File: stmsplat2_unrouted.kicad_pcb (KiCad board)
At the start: 2 copper layers, 100 x 100 mm, 107 parts, among them J1 C11_2X36, J10 Conn_01x03_Male, J11 Conn_01x02_Male, J12 Conn_01x04_Male, J13 Conn_01x04_Male, J14 Conn_01x02, J15 Conn_01x02, J16 Screw_Terminal_01x03, J17 Screw_Terminal_01x02, J2 C12_2X36, J3 Conn_01x04_Male, J4 Conn_01x04_Male, J5 Conn_Coaxial, J6 Conn_01x04_Male, J7 Conn_01x04_Male, J8 Conn_01x04_Male, J9 Conn_01x03_Male, Q1 BSS138LT1G, U1 ublox_chinese_PCB_module, U10 XCVR_E30-400M20S (Si4463), U11 3115_module, U2 ESP-C3-13U, U3 SST25VF032B, U4 48L512-48LM01, U5 Opamp_Quad_MCP6024, U6 E180-ZG120A, U7 AZ1084C, U8 MCP6S93-X_UN, U9 DS2485

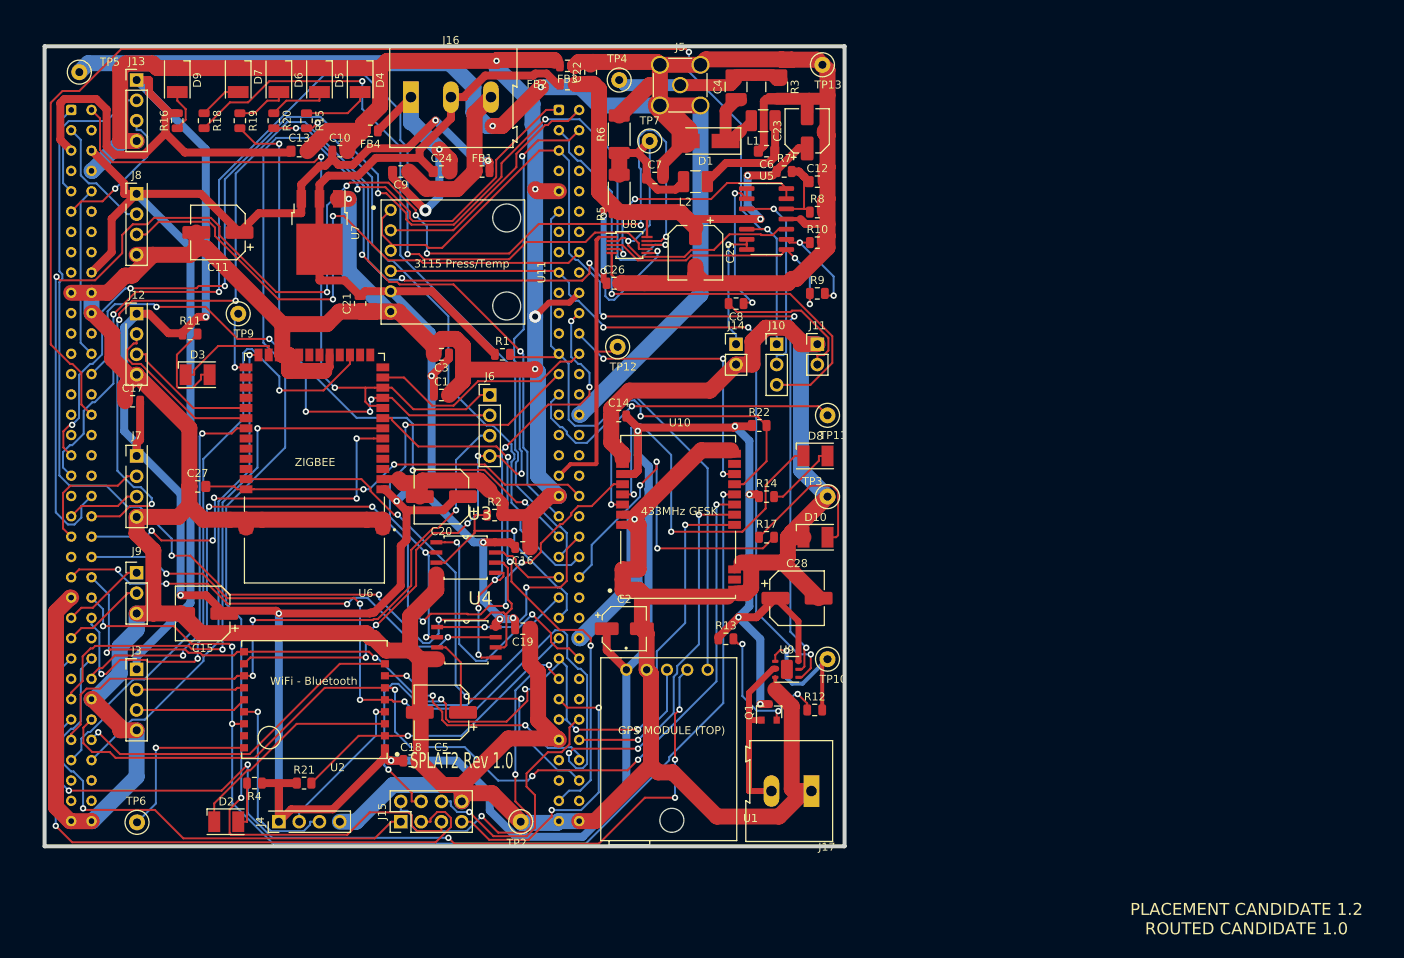
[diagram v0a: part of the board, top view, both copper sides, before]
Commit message: Few footprints changes, placement changes, initial routing success
SCH: 0.11 (now feature frozen)
PCB: Placement 1.2
PCB Routed 1.0
The unrouted pcb is also in this folder
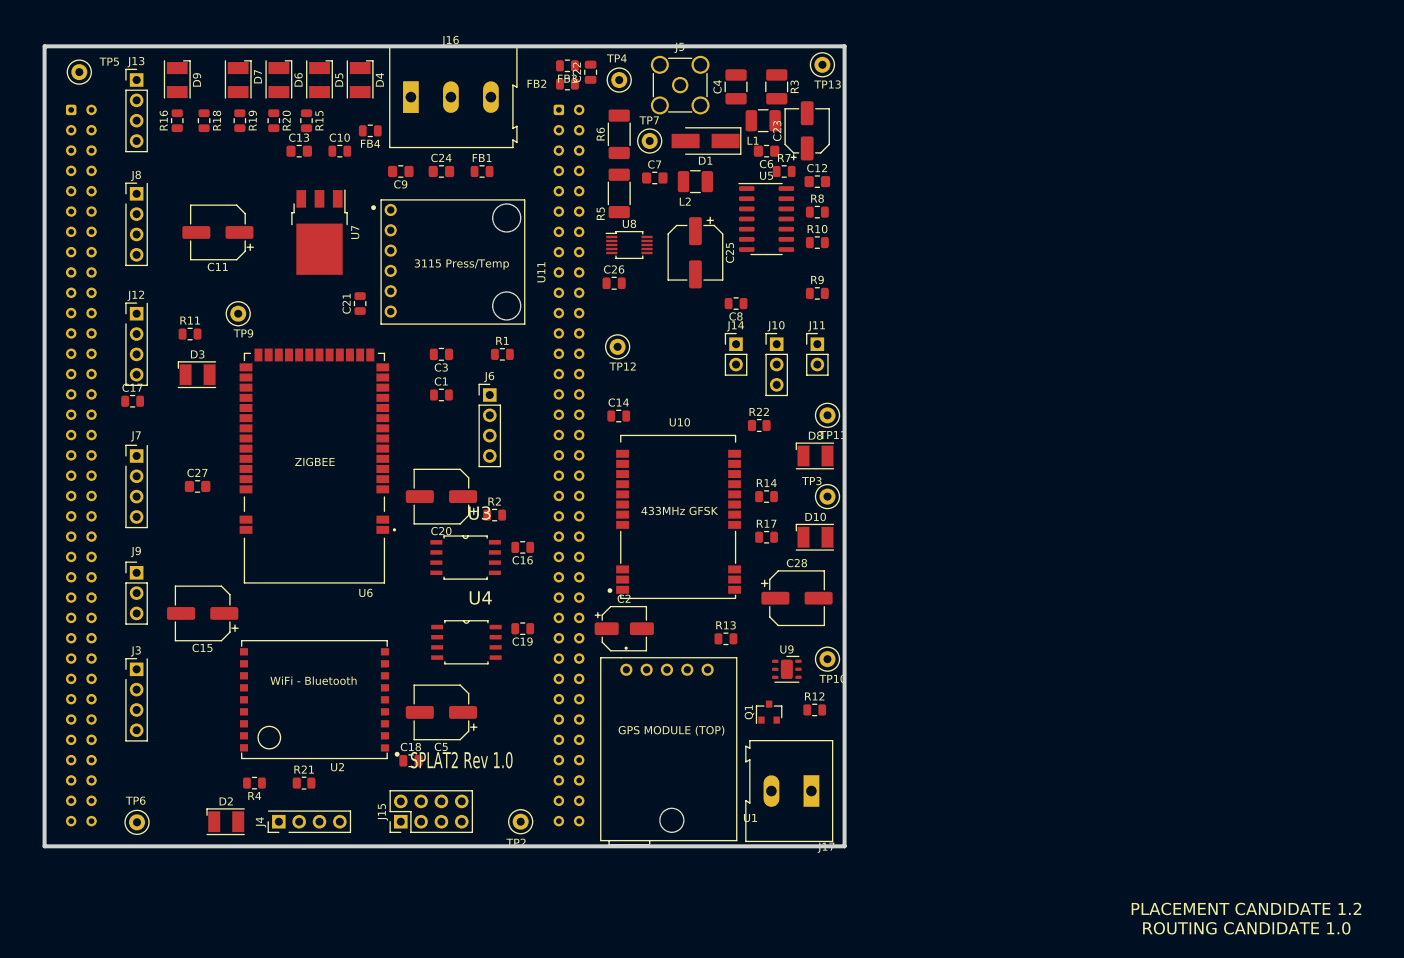
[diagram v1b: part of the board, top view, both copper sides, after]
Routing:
- net GND: track 827.8 -> 0.00 mm, vias 6 -> 0
- net VDD: track 569.3 -> 0.00 mm, vias 14 -> 0
- net GNDA: track 275.5 -> 0.00 mm, vias 2 -> 0
- net PC9: track 171.4 -> 0.00 mm, vias 2 -> 0
- net PD3: track 168.7 -> 0.00 mm, vias 7 -> 0
- net PA4: track 168.1 -> 0.00 mm, vias 2 -> 0
- net PE2: track 145.6 -> 0.00 mm, vias 7 -> 0
- net +5V: track 144.8 -> 0.00 mm, vias 2 -> 0
- net PG2: track 143.9 -> 0.00 mm, vias 6 -> 0
- net PE5: track 140.9 -> 0.00 mm, vias 4 -> 0
- net PC2: track 140.6 -> 0.00 mm, vias 6 -> 0
- net PC3: track 132.9 -> 0.00 mm, vias 3 -> 0
- net PE13: track 130.1 -> 0.00 mm, vias 7 -> 0
- net PC10: track 129.0 -> 0.00 mm, vias 3 -> 0
- net PB9: track 125.0 -> 0.00 mm, vias 3 -> 0
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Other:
- board text added: "PLACEMENT CANDIDATE 1.2 ROUTING CANDIDATE 1.0"
- board text removed: "PLACEMENT CANDIDATE 1.2 ROUTED CANDIDATE 1.0"

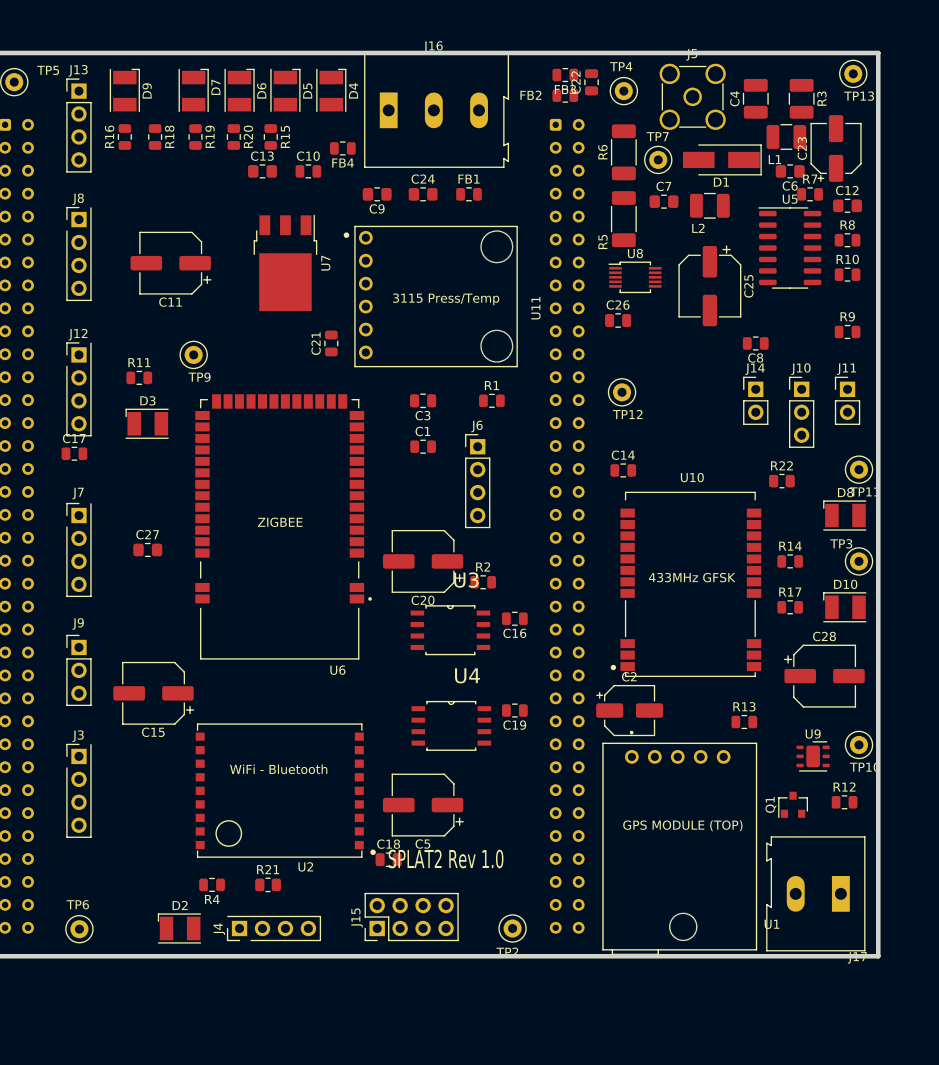
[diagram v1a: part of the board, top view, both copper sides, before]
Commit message: SPI2<->SPI3. Different placement. Routed, but may have other errors
Swapped SPI2 and SPI3 and have added termination for SPI2 (which may not be needed)/ Moved RAM/ROM components close to the connector
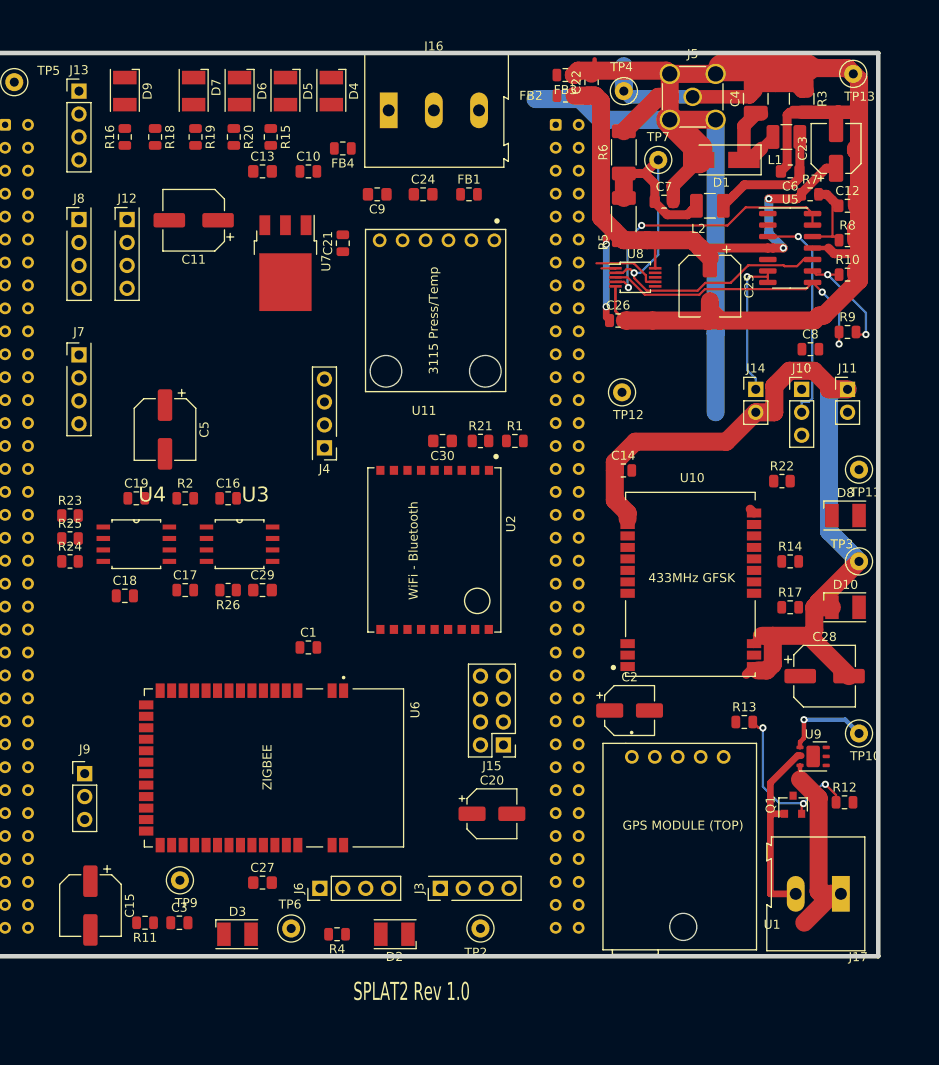
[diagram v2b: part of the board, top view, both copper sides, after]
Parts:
- added C29: 470pF, Capacitor_SMD:C_0805_2012Metric_Pad1.15x1.40mm_HandSolder, F.Cu at (83.8, 125.1)
- added C30: 0.1uF, Capacitor_SMD:C_0805_2012Metric_Pad1.15x1.40mm_HandSolder, F.Cu at (103.8, 108.6)
- added R23: 50R, Resistor_SMD:R_0805_2012Metric, F.Cu at (62.5, 116.8)
- added R24: 33R, Resistor_SMD:R_0805_2012Metric, F.Cu at (62.5, 121.9)
- added R25: 50R, Resistor_SMD:R_0805_2012Metric, F.Cu at (62.5, 119.4)
- added R26: 110R, Resistor_SMD:R_0805_2012Metric, F.Cu at (80.0, 125.1)
- C20: footprint Capacitor_SMD:CP_Elec_6.3x7.7 -> Capacitor_SMD:CP_Elec_5x5.4
- moved C3 63.8 mm to (74.6, 161.9), turned to 0 degrees
- moved R11 60.3 mm to (70.8, 161.9), turned to 180 degrees
- moved TP9 58.2 mm to (74.7, 157.2)
- moved D3 57.4 mm to (81.0, 163.2)
- moved R21 54.5 mm to (108.0, 108.6)
- moved J4 54.0 mm to (90.7, 109.3), turned to 180 degrees
- moved J6 51.9 mm to (90.2, 158.1), turned to 90 degrees
- moved C5 50.5 mm to (73.0, 107.3), turned to 270 degrees
- moved C19 48.0 mm to (69.8, 114.9), turned to 0 degrees
- moved J3 42.6 mm to (103.5, 158.1), turned to 90 degrees
- moved C18 41.3 mm to (68.6, 125.7)
- moved U4 40.3 mm to (69.8, 120.0)
- moved C27 39.0 mm to (83.8, 157.5)
- moved C16 34.4 mm to (80.0, 114.9), turned to 0 degrees
- moved R2 34.3 mm to (75.3, 114.9)
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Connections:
- U3 pad 2: PB4 -> /SPI2_MISOT
- U3 pad 5: PB2 -> /SPI2_MOSIT
- U3 pad 6: PC10 -> /SPI2_SCKT
- U4 pad 2: PB4 -> /SPI2_MISOT
- U4 pad 5: PB2 -> /SPI2_MOSIT
- U4 pad 6: PC10 -> /SPI2_SCKT
- U8 pad 7: PC3 -> PB2
- U8 pad 8: PC2 -> PB4
- U8 pad 9: PD3 -> PC10
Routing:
- net GNDA: track 0.00 -> 197.6 mm
- net GND: track 0.00 -> 117.1 mm
- net A3V3: track 0.00 -> 69.9 mm, vias 0 -> 4
- net Net-(C7-Pad1): track 0.00 -> 56.1 mm, vias 0 -> 1
- net Net-(R9-Pad1): track 0.00 -> 32.5 mm, vias 0 -> 2
- net /HALF3V3: track 0.00 -> 30.7 mm, vias 0 -> 2
- net Net-(C4-Pad2): track 0.00 -> 27.8 mm
- net Net-(J10-Pad2): track 0.00 -> 24.4 mm, vias 0 -> 1
- net Net-(J17-Pad2): track 0.00 -> 21.5 mm
- net Net-(Q1-Pad2): track 0.00 -> 20.2 mm, vias 0 -> 3
- net Net-(J14-Pad1): track 0.00 -> 16.4 mm, vias 0 -> 1
- net Net-(C6-Pad1): track 0.00 -> 15.9 mm
- net Net-(R10-Pad1): track 0.00 -> 12.7 mm, vias 0 -> 2
- net Net-(C4-Pad1): track 0.00 -> 11.1 mm
- net Net-(R12-Pad2): track 0.00 -> 9.97 mm, vias 0 -> 2
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
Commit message: Routing attempt
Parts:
- moved C13 15.5 mm to (68.3, 78.7), turned to 180 degrees
- moved FB1 11.5 mm to (95.2, 80.0), turned to 180 degrees
- moved C9 10.5 mm to (106.9, 80.0)
- moved FB4 7.62 mm to (92.7, 68.6)
- moved TP10 4.58 mm to (147.3, 144.8)
- moved R15 4.17 mm to (88.9, 74.9)
- moved U2 3.81 mm to (99.1, 120.7), turned to 0 degrees
- moved R20 3.17 mm to (83.8, 74.9)
- moved D5 2.54 mm to (83.8, 69.8)
- moved D6 2.54 mm to (78.7, 69.8)
- moved D7 2.54 mm to (73.7, 69.8)
- moved D4 2.54 mm to (88.9, 69.8)
- moved R19 2.34 mm to (78.7, 74.9)
- moved R12 1.80 mm to (147.0, 149.9)
- moved U9 1.80 mm to (143.5, 142.2), turned to 180 degrees
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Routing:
- net GND: track 117.1 -> 840.3 mm, vias 0 -> 8
- net VDD: track 0.00 -> 549.0 mm, vias 0 -> 9
- net +5V: track 0.00 -> 154.4 mm, vias 0 -> 1
- net PE13: track 0.00 -> 140.7 mm, vias 0 -> 4
- net PD14: track 0.00 -> 140.3 mm, vias 0 -> 6
- net PC11: track 0.00 -> 134.5 mm, vias 0 -> 4
- net PA4: track 0.00 -> 134.1 mm, vias 0 -> 1
- net Net-(J12-Pad2): track 0.00 -> 115.9 mm, vias 0 -> 5
- net PG9: track 0.00 -> 112.0 mm, vias 0 -> 2
- net PE8: track 0.00 -> 109.3 mm, vias 0 -> 1
- net PD11: track 0.00 -> 107.5 mm, vias 0 -> 5
- net Net-(J12-Pad3): track 0.00 -> 106.0 mm, vias 0 -> 1
- net PB9: track 0.00 -> 103.2 mm, vias 0 -> 2
- net PC9: track 0.00 -> 102.4 mm, vias 0 -> 3
- net PC6: track 0.00 -> 101.4 mm, vias 0 -> 1
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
